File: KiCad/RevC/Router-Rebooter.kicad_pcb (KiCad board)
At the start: 2 copper layers, 62 x 49 mm, 18 parts, among them J1 12V Out, J2 ESP32 Power Bypass, J3 12V In, K1 OMRON G5LE-1-VD, Q1 PN2222A, U1 PSU2-5, U2 ESP32-C3-Zero

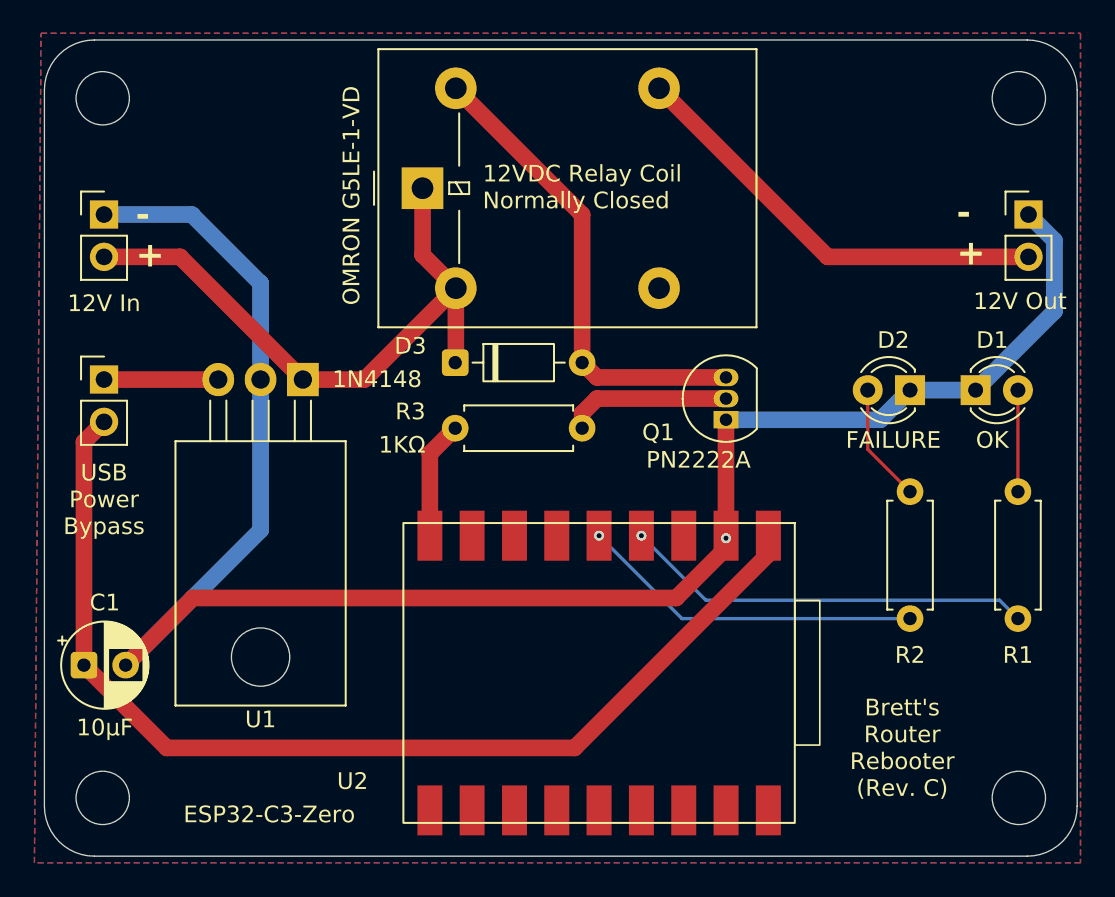
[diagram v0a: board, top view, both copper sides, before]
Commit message: Small PCB adjustments
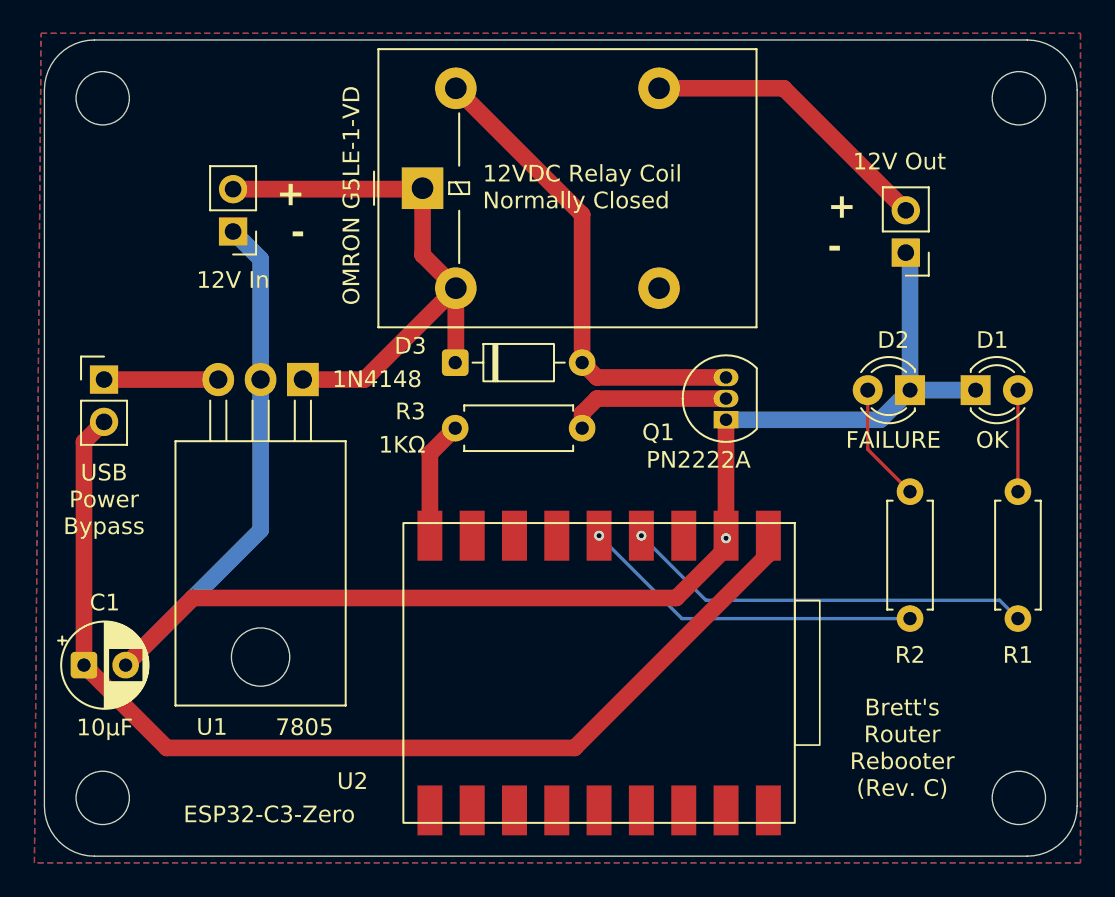
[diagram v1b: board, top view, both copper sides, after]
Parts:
- moved J3 7.81 mm to (69.0, 44.0), turned to 180 degrees
- moved J1 7.71 mm to (109.4, 45.3), turned to 180 degrees
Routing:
- net GND: track 112.9 -> 100.8 mm
- net /+12V_{OUT}: track 26.4 -> 17.8 mm
- net /+12V_{IN}: track 37.8 -> 34.2 mm
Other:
- board text added: "+ -"
- board text added: "7805"
- board text added: "USB Power Bypass Open: ESP32 powered via USB Closed: ESP32 powered via 12V input"
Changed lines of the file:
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@@
 		(tags "TO-220-3 Horizontal RM 2.54mm")
 		(property "Reference" "U1"
-			(at 2.54 -20.41 0)
+			(at 5.461 -20.86125 0)
 			(layer "F.SilkS")
 			(effects
@@
 			(at 2.54 1.95 0)
 			(layer "F.Fab")
+			(hide yes)
 			(effects
 				(font
@@
 	(footprint "Connector_PinHeader_2.54mm:PinHeader_1x02_P2.54mm_Vertical"
 		(layer "F.Cu")
-		(at 116.7954 43.0274)
+		(at 109.4294 45.3134 180)
 		(descr "Through hole straight pin header, 1x02, 2.54mm pitch, single row")
 		(tags "Through hole pin header THT 1x02 2.54mm single row")
@@
 		)
 		(property "Value" "12V Out"
-			(at -0.508 5.207 0)
+			(at 0.381 5.461 0)
 			(layer "F.SilkS")
 			(effects
@@
 		(attr through_hole)
 		(fp_line
-			(start -1.38 -1.38)
-			(end 0 -1.38)
+			(start 1.38 1.27)
+			(end 1.38 3.92)
 			(stroke
 				(width 0.12)
@@
 		)
 		(fp_line
-			(start -1.38 0)
-			(end -1.38 -1.38)
+			(start -1.38 3.92)
+			(end 1.38 3.92)
 			(stroke
 				(width 0.12)
@@
 		(fp_line
 			(start -1.38 1.27)
-			(end -1.38 3.92)
+			(end 1.38 1.27)
 			(stroke
 				(width 0.12)
@@
 		(fp_line
 			(start -1.38 1.27)
-			(end 1.38 1.27)
+			(end -1.38 3.92)
 			(stroke
 				(width 0.12)
@@
 		)
 		(fp_line
-			(start -1.38 3.92)
-			(end 1.38 3.92)
+			(start -1.38 0)
+			(end -1.38 -1.38)
 			(stroke
 				(width 0.12)
@@
 		)
 		(fp_line
-			(start 1.38 1.27)
-			(end 1.38 3.92)
+			(start -1.38 -1.38)
+			(end 0 -1.38)
 			(stroke
 				(width 0.12)
@@
 		)
 		(fp_line
-			(start -1.77 -1.77)
-			(end -1.77 4.32)
+			(start 1.77 4.32)
+			(end 1.77 -1.77)
 			(stroke
 				(width 0.05)
@@
 		)
 		(fp_line
-			(start -1.77 4.32)
-			(end 1.77 4.32)
+			(start 1.77 -1.77)
+			(end -1.77 -1.77)
 			(stroke
 				(width 0.05)
@@
 		)
 		(fp_line
-			(start 1.77 -1.77)
-			(end -1.77 -1.77)
+			(start -1.77 4.32)
+			(end 1.77 4.32)
 			(stroke
 				(width 0.05)
@@
 		)
 		(fp_line
-			(start 1.77 4.32)
-			(end 1.77 -1.77)
+			(start -1.77 -1.77)
+			(end -1.77 4.32)
 			(stroke
 				(width 0.05)
@@
 		)
 		(fp_line
-			(start -1.27 -0.635)
-			(end -0.635 -1.27)
+			(start 1.27 3.81)
+			(end -1.27 3.81)
 			(stroke
 				(width 0.1)
@@
 		)
 		(fp_line
-			(start -1.27 3.81)
-			(end -1.27 -0.635)
+			(start 1.27 -1.27)
+			(end 1.27 3.81)
 			(stroke
 				(width 0.1)
@@
 		)
 		(fp_line
-			(start 1.27 -1.27)
-			(end 1.27 3.81)
+			(start -1.27 3.81)
+			(end -1.27 -0.635)
 			(stroke
 				(width 0.1)
@@
 		)
 		(fp_line
-			(start 1.27 3.81)
-			(end -1.27 3.81)
+			(start -1.27 -0.635)
+			(end -0.635 -1.27)
 			(stroke
 				(width 0.1)
@@
 		)
 		(pad "1" thru_hole rect
-			(at 0 0)
+			(at 0 0 180)
 			(size 1.7 1.7)
 			(drill 1)
@@
 		)
 		(pad "2" thru_hole circle
-			(at 0 2.54)
+			(at 0 2.54 180)
 			(size 1.7 1.7)
 			(drill 1)
@@
 	(footprint "Connector_PinHeader_2.54mm:PinHeader_1x02_P2.54mm_Vertical"
 		(layer "F.Cu")
-		(at 61.2964 43.0274)
+		(at 69.0434 44.0434 180)
 		(descr "Through hole straight pin header, 1x02, 2.54mm pitch, single row")
 		(tags "Through hole pin header THT 1x02 2.54mm single row")
@@
 		)
 		(property "Value" "12V In"
-			(at 0 5.334 0)
+			(at 0 -2.921 0)
 			(layer "F.SilkS")
 			(effects
@@
 		(attr through_hole)
 		(fp_line
-			(start -1.38 -1.38)
-			(end 0 -1.38)
+			(start 1.38 1.27)
+			(end 1.38 3.92)
 			(stroke
 				(width 0.12)
@@
 		)
 		(fp_line
-			(start -1.38 0)
-			(end -1.38 -1.38)
+			(start -1.38 3.92)
+			(end 1.38 3.92)
 			(stroke
 				(width 0.12)
@@
 		(fp_line
 			(start -1.38 1.27)
-			(end -1.38 3.92)
+			(end 1.38 1.27)
 			(stroke
 				(width 0.12)
@@
 		(fp_line
 			(start -1.38 1.27)
-			(end 1.38 1.27)
+			(end -1.38 3.92)
 			(stroke
 				(width 0.12)
@@
 		)
 		(fp_line
-			(start -1.38 3.92)
-			(end 1.38 3.92)
+			(start -1.38 0)
+			(end -1.38 -1.38)
 			(stroke
 				(width 0.12)
@@
 		)
 		(fp_line
-			(start 1.38 1.27)
-			(end 1.38 3.92)
+			(start -1.38 -1.38)
+			(end 0 -1.38)
 			(stroke
 				(width 0.12)
@@
 		)
 		(fp_line
-			(start -1.77 -1.77)
-			(end -1.77 4.32)
+			(start 1.77 4.32)
+			(end 1.77 -1.77)
 			(stroke
 				(width 0.05)
@@
 		)
 		(fp_line
-			(start -1.77 4.32)
-			(end 1.77 4.32)
+			(start 1.77 -1.77)
+			(end -1.77 -1.77)
 			(stroke
 				(width 0.05)
@@
 		)
 		(fp_line
-			(start 1.77 -1.77)
-			(end -1.77 -1.77)
+			(start -1.77 4.32)
+			(end 1.77 4.32)
 			(stroke
 				(width 0.05)
@@
 		)
 		(fp_line
-			(start 1.77 4.32)
-			(end 1.77 -1.77)
+			(start -1.77 -1.77)
+			(end -1.77 4.32)
 			(stroke
 				(width 0.05)
@@
 		)
 		(fp_line
-			(start -1.27 -0.635)
-			(end -0.635 -1.27)
+			(start 1.27 3.81)
+			(end -1.27 3.81)
 			(stroke
 				(width 0.1)
@@
 		)
 		(fp_line
-			(start -1.27 3.81)
-			(end -1.27 -0.635)
+			(start 1.27 -1.27)
+			(end 1.27 3.81)
 			(stroke
 				(width 0.1)
@@
 		)
 		(fp_line
-			(start 1.27 -1.27)
-			(end 1.27 3.81)
+			(start -1.27 3.81)
+			(end -1.27 -0.635)
 			(stroke
 				(width 0.1)
@@
 		)
 		(fp_line
-			(start 1.27 3.81)
-			(end -1.27 3.81)
+			(start -1.27 -0.635)
+			(end -0.635 -1.27)
 			(stroke
 				(width 0.1)
@@
 		)
 		(pad "1" thru_hole rect
-			(at 0 0)
+			(at 0 0 180)
 			(size 1.7 1.7)
 			(drill 1)
@@
 		)
 		(pad "2" thru_hole circle
-			(at 0 2.54)
+			(at 0 2.54 180)
 			(size 1.7 1.7)
 			(drill 1)
@@
 		)
 	)
-	(gr_text "-\n+"
-		(at 112.4774 46.2024 0)
+	(gr_text "+\n-"
+		(at 104.7304 45.8214 0)
 		(layer "F.SilkS")
 		(effects
@@
 	)
 	(gr_text "-\n+"
-		(at 63.2014 46.3294 0)
+		(at 73.3614 40.9954 180)
 		(layer "F.SilkS")
 		(effects
@@
 		)
 	)
+	(gr_text "7805"
+		(at 71.5834 74.3964 0)
+		(layer "F.SilkS")
+		(effects
+			(font
+				(size 1 1)
+				(thickness 0.15)
+			)
+			(justify left bottom)
+		)
+	)
 	(gr_text "12VDC Relay Coil\nNormally Closed"
 		(at 84.0294 42.7734 0)
@@
 		)
 	)
+	(gr_text "USB Power Bypass\nOpen:   ESP32 powered via USB\nClosed: ESP32 powered via 12V input"
+		(at 66.8844 46.9644 90)
+		(layer "B.SilkS")
+		(effects
+			(font
+				(size 1 1)
+				(thickness 0.1)
+			)
+			(justify left bottom mirror)
+		)
+	)
 	(segment
 		(start 116.1604 59.6644)
@@
 	)
 	(segment
-		(start 61.2964 45.5674)
-		(end 65.8684 45.5674)
+		(start 80.3604 41.5034)
+		(end 80.4164 41.4474)
 		(width 1)
 		(layer "F.Cu")
@@
 	)
 	(segment
-		(start 65.8684 45.5674)
-		(end 73.2344 52.9334)
+		(start 80.4164 45.4474)
+		(end 82.4164 47.4474)
 		(width 1)
 		(layer "F.Cu")
@@
 	)
 	(segment
-		(start 80.4164 45.4474)
-		(end 82.4164 47.4474)
+		(start 69.0434 41.5034)
+		(end 80.3604 41.5034)
 		(width 1)
 		(layer "F.Cu")
@@
 	)
 	(segment
-		(start 118.3464 44.5784)
-		(end 116.7954 43.0274)
-		(width 1)
-		(layer "B.Cu")
-		(net 3)
-	)
-	(segment
-		(start 66.5694 43.0274)
-		(end 70.6944 47.1524)
-		(width 1)
-		(layer "B.Cu")
-		(net 3)
-	)
-	(segment
 		(start 107.9054 55.3464)
 		(end 109.6834 53.5684)
@@
 	)
 	(segment
-		(start 61.2964 43.0274)
-		(end 66.5694 43.0274)
+		(start 109.6834 53.5684)
+		(end 109.6834 45.5674)
 		(width 1)
 		(layer "B.Cu")
@@
 	)
 	(segment
-		(start 70.6944 61.975288)
-		(end 62.591288 70.0784)
+		(start 109.6834 45.5674)
+		(end 109.4294 45.3134)
 		(width 1)
 		(layer "B.Cu")
@@
 	)
 	(segment
-		(start 70.6944 47.1524)
-		(end 70.6944 52.9334)
+		(start 70.6944 45.6944)
+		(end 69.0434 44.0434)
 		(width 1)
 		(layer "B.Cu")
@@
 	)
 	(segment
-		(start 118.3464 48.8424)
-		(end 118.3464 44.5784)
+		(start 70.6944 61.975288)
+		(end 62.591288 70.0784)
 		(width 1)
 		(layer "B.Cu")
@@
 	)
 	(segment
-		(start 113.6204 53.5684)
-		(end 118.3464 48.8424)
+		(start 70.6944 52.9334)
+		(end 70.6944 45.6944)
 		(width 1)
 		(layer "B.Cu")
@@
 	)
 	(segment
-		(start 104.7364 45.5674)
-		(end 116.7954 45.5674)
+		(start 94.6164 35.4474)
+		(end 102.1034 35.4474)
 		(width 1)
 		(layer "F.Cu")
@@
 	)
 	(segment
-		(start 94.6164 35.4474)
-		(end 104.7364 45.5674)
+		(start 102.1034 35.4474)
+		(end 109.4294 42.7734)
 		(width 1)
 		(layer "F.Cu")

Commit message: Re-oriented the PCB
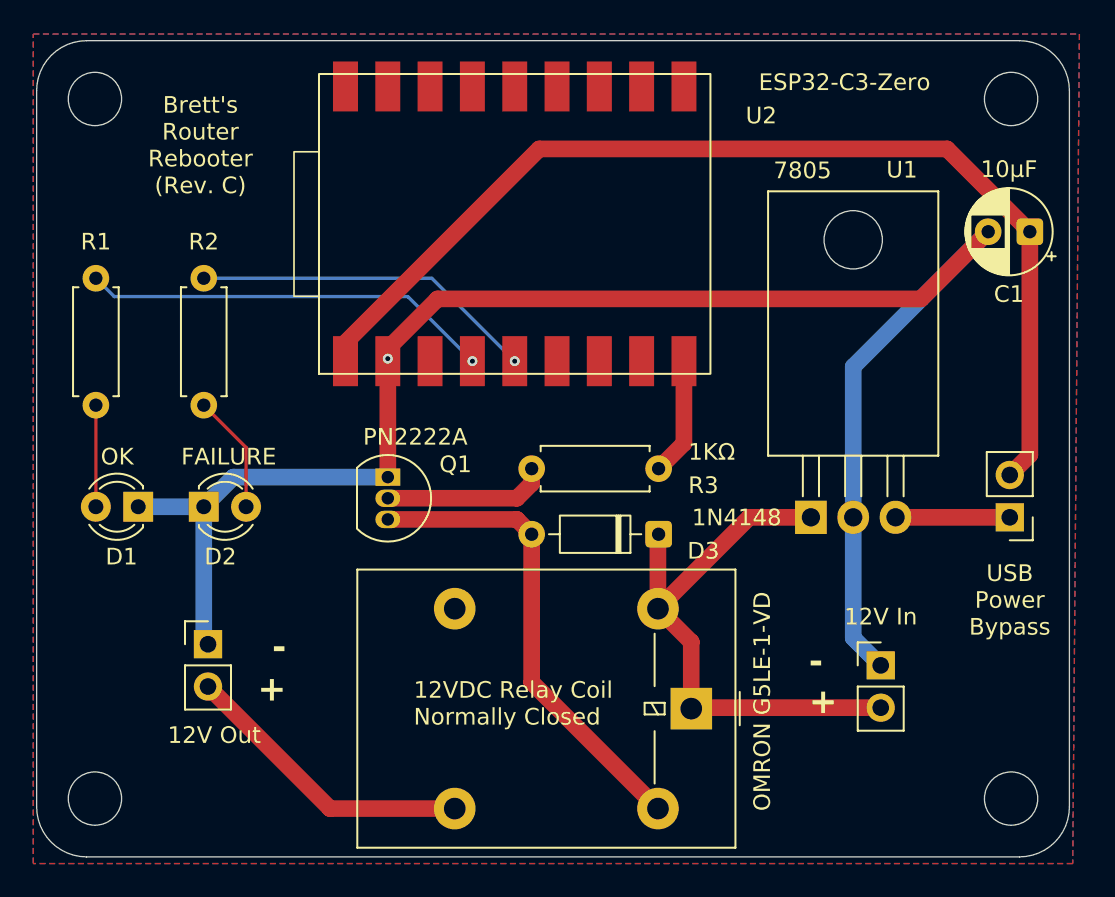
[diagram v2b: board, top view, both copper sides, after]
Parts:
- moved H2 69.6 mm to (60.8, 78.1), turned to 180 degrees
- moved H1 69.5 mm to (60.8, 36.1), turned to 180 degrees
- moved H4 68.9 mm to (115.8, 78.1), turned to 180 degrees
- moved H3 68.8 mm to (115.8, 36.1), turned to 180 degrees
- moved C1 62.5 mm to (116.9, 44.1), turned to 180 degrees
- moved R1 59.0 mm to (60.8, 46.9), turned to -90 degrees
- moved J2 55.0 mm to (115.7, 61.2), turned to 180 degrees
- moved D1 50.8 mm to (63.3, 60.6), turned to 180 degrees
- moved J1 48.0 mm to (67.5, 68.8), turned to 0 degrees
- moved R2 47.1 mm to (67.3, 46.9), turned to -90 degrees
- moved J3 46.8 mm to (107.9, 70.1), turned to 0 degrees
- moved D2 43.0 mm to (67.3, 60.6), turned to 0 degrees
- moved K1 35.2 mm to (96.6, 72.7), turned to -90 degrees
- moved U1 31.6 mm to (103.7, 61.2), turned to 0 degrees
- moved U2 26.5 mm to (85.7, 44.1), turned to 90 degrees
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
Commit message: Artwork update
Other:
- board text added: "PSU2-5"
- board text removed: "7805"

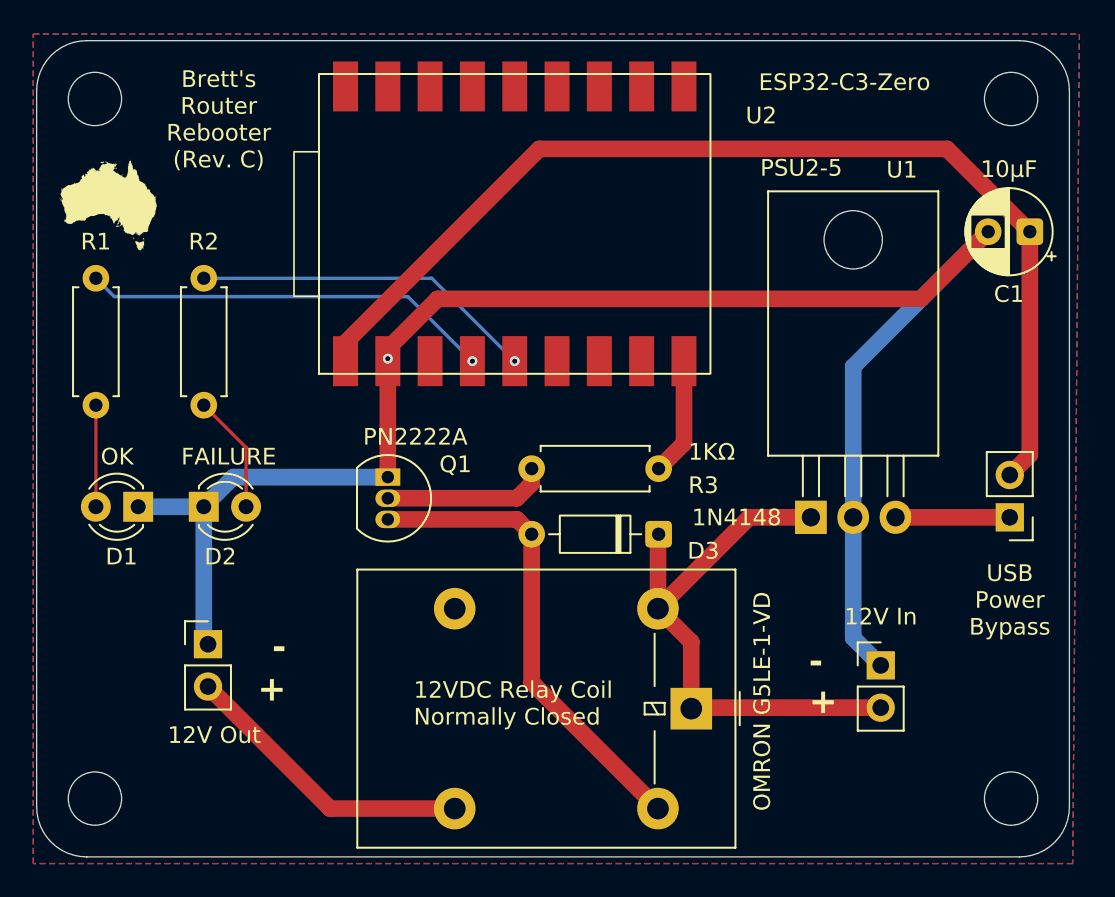
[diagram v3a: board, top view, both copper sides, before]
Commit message: Replaced D3, added D4
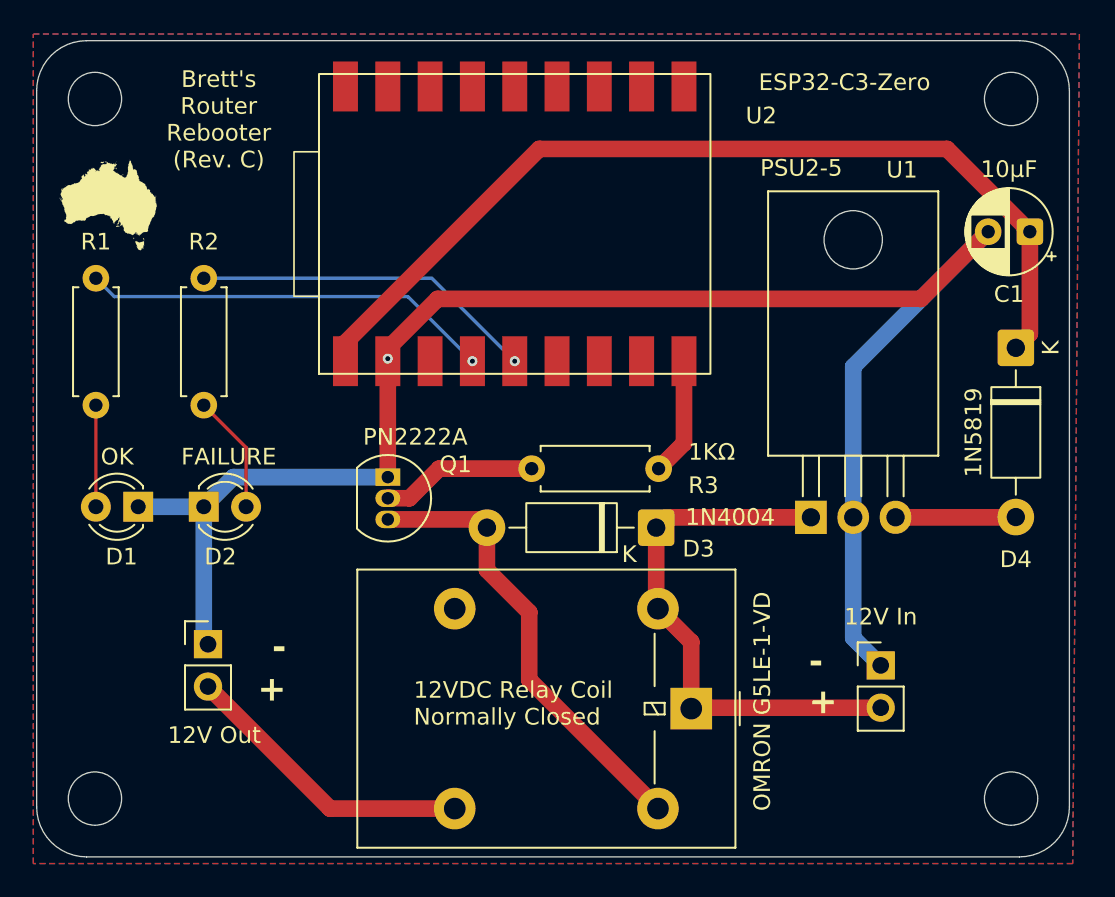
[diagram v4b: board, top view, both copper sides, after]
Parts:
- removed J2: ESP32 Power Bypass, Connector_PinHeader_2.54mm:PinHeader_1x02_P2.54mm_Vertical
- added D4: 1N5819, Diode_THT:D_DO-41_SOD81_P10.16mm_Horizontal, F.Cu at (116.0, 51.0)
- D3: value 1N4148 -> 1N4004; footprint Diode_THT:D_DO-35_SOD27_P7.62mm_Horizontal -> Diode_THT:D_DO-41_SOD81_P10.16mm_Horizontal
- moved D3 0.42 mm to (94.4, 61.8)
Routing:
- net +5V_{ESP32}: track 64.2 -> 56.4 mm
- net /+12V_{IN}: track 34.2 -> 32.7 mm
- net Net-(D3-A): track 28.6 -> 27.3 mm
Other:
- board text removed: "USB Power Bypass"

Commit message: Added user text to PCB
Clarify the empty zone on PCB is where the ESP32's WiFi antenna is so should be kept clear (this is for the PCB fab)
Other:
- board text added: "ESP32 WiFi antenna zone Leave clear"
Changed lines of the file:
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@@
+		)
+	)
+	(gr_text "ESP32\nWiFi\nantenna\nzone\nLeave\nclear"
+		(at 94.4434 47.2184 0)
+		(layer "Cmts.User")
+		(effects
+			(font
+				(size 0.8 0.6)
+				(thickness 0.075)
+			)
+			(justify left bottom)
 		)
 	)
